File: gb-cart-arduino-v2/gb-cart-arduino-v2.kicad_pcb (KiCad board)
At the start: 2 copper layers, 58.5 x 53 mm, 18 parts, among them J1 Conn_01x16_Pin, U1 74HC595, U2 74HC595

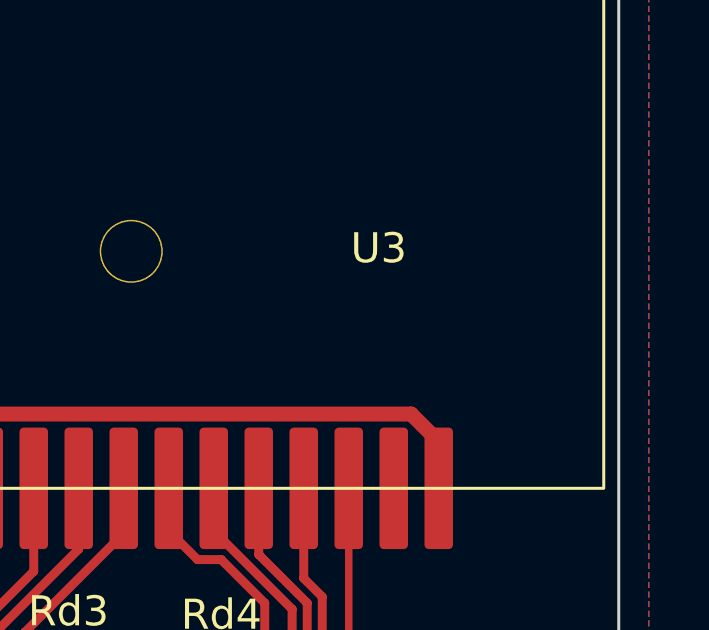
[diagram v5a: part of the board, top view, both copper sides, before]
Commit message: Moved connector definition to project
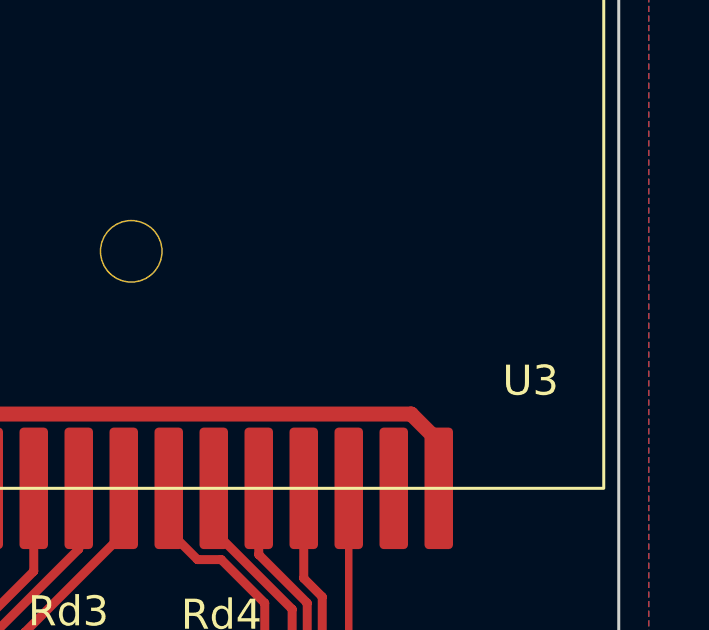
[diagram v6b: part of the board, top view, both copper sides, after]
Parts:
- U3: footprint 1_my_custom_library:Gameboy cartridge connector -> gb-cart:Gameboy cartridge connector
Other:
- board text added: "https://github.com/GreenOlvi/gb-cart-reader-schematics"
- board text added: "v2.1"
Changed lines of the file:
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@@
 		)
 	)
-	(footprint "1_my_custom_library:Gameboy cartridge connector"
+	(footprint "gb-cart:Gameboy cartridge connector"
 		(layer "F.Cu")
 		(at 133.5 101)
 		(property "Reference" "U3"
-			(at -2 -8 0)
+			(at 4 -3 0)
 			(unlocked yes)
 			(layer "F.SilkS")
@@
 					(thickness 0.1)
 				)
+				(justify right bottom)
 			)
 		)
 		(property "Value" "~"
-			(at -2 -6 0)
+			(at 0 -18.5 0)
 			(unlocked yes)
 			(layer "F.Fab")
@@
 		)
 		(fp_text user "${REFERENCE}"
-			(at -1 -4 0)
+			(at -1 -16.5 0)
 			(unlocked yes)
 			(layer "F.Fab")
@@
 		)
 	)
+	(gr_text "v2.1"
+		(at 137.5 82.5 0)
+		(layer "B.SilkS")
+		(effects
+			(font
+				(size 1 1)
+				(thickness 0.15)
+			)
+			(justify left bottom mirror)
+		)
+	)
+	(gr_text "https://github.com/GreenOlvi/gb-cart-reader-schematics"
+		(at 138 80 0)
+		(layer "B.SilkS")
+		(effects
+			(font
+				(size 1 1)
+				(thickness 0.15)
+			)
+			(justify left bottom mirror)
+		)
+	)
